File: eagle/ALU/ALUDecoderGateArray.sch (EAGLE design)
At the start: 0 parts

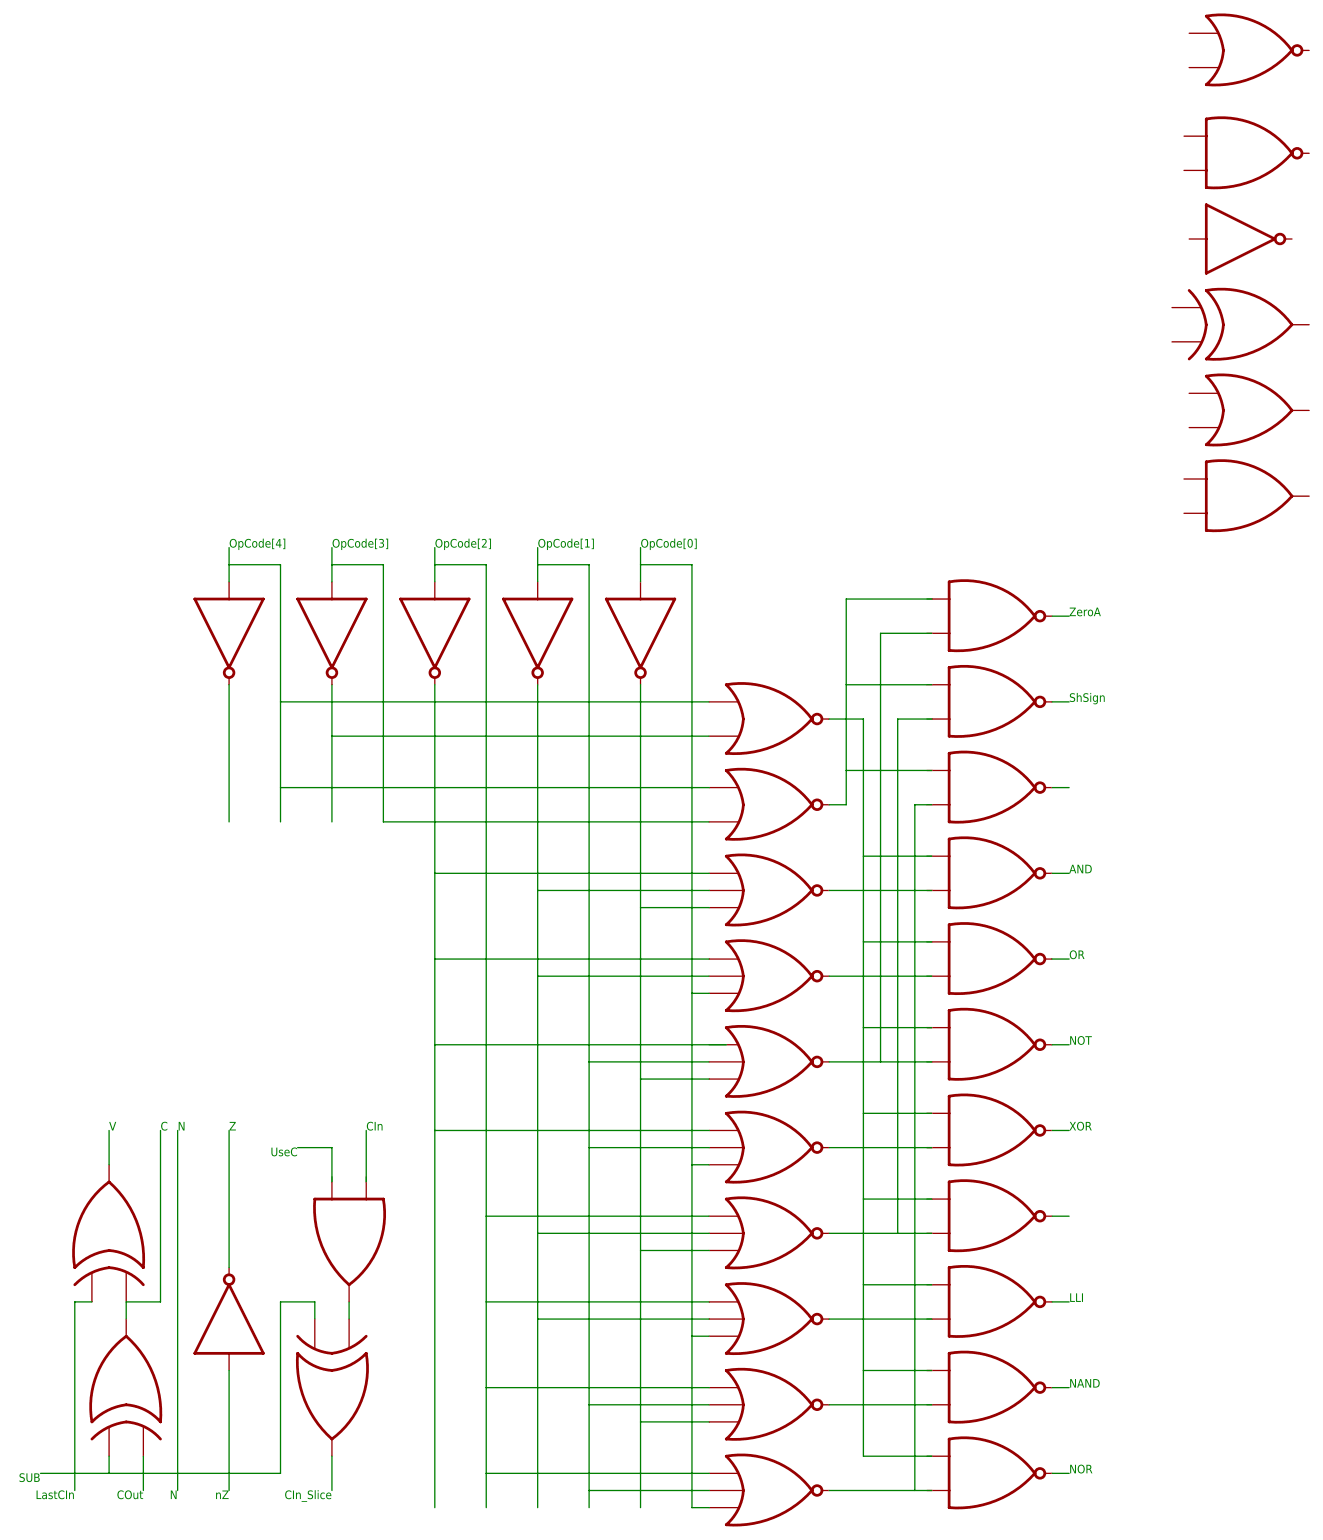
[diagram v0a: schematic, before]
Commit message: FR:ALU design reduction and rewording
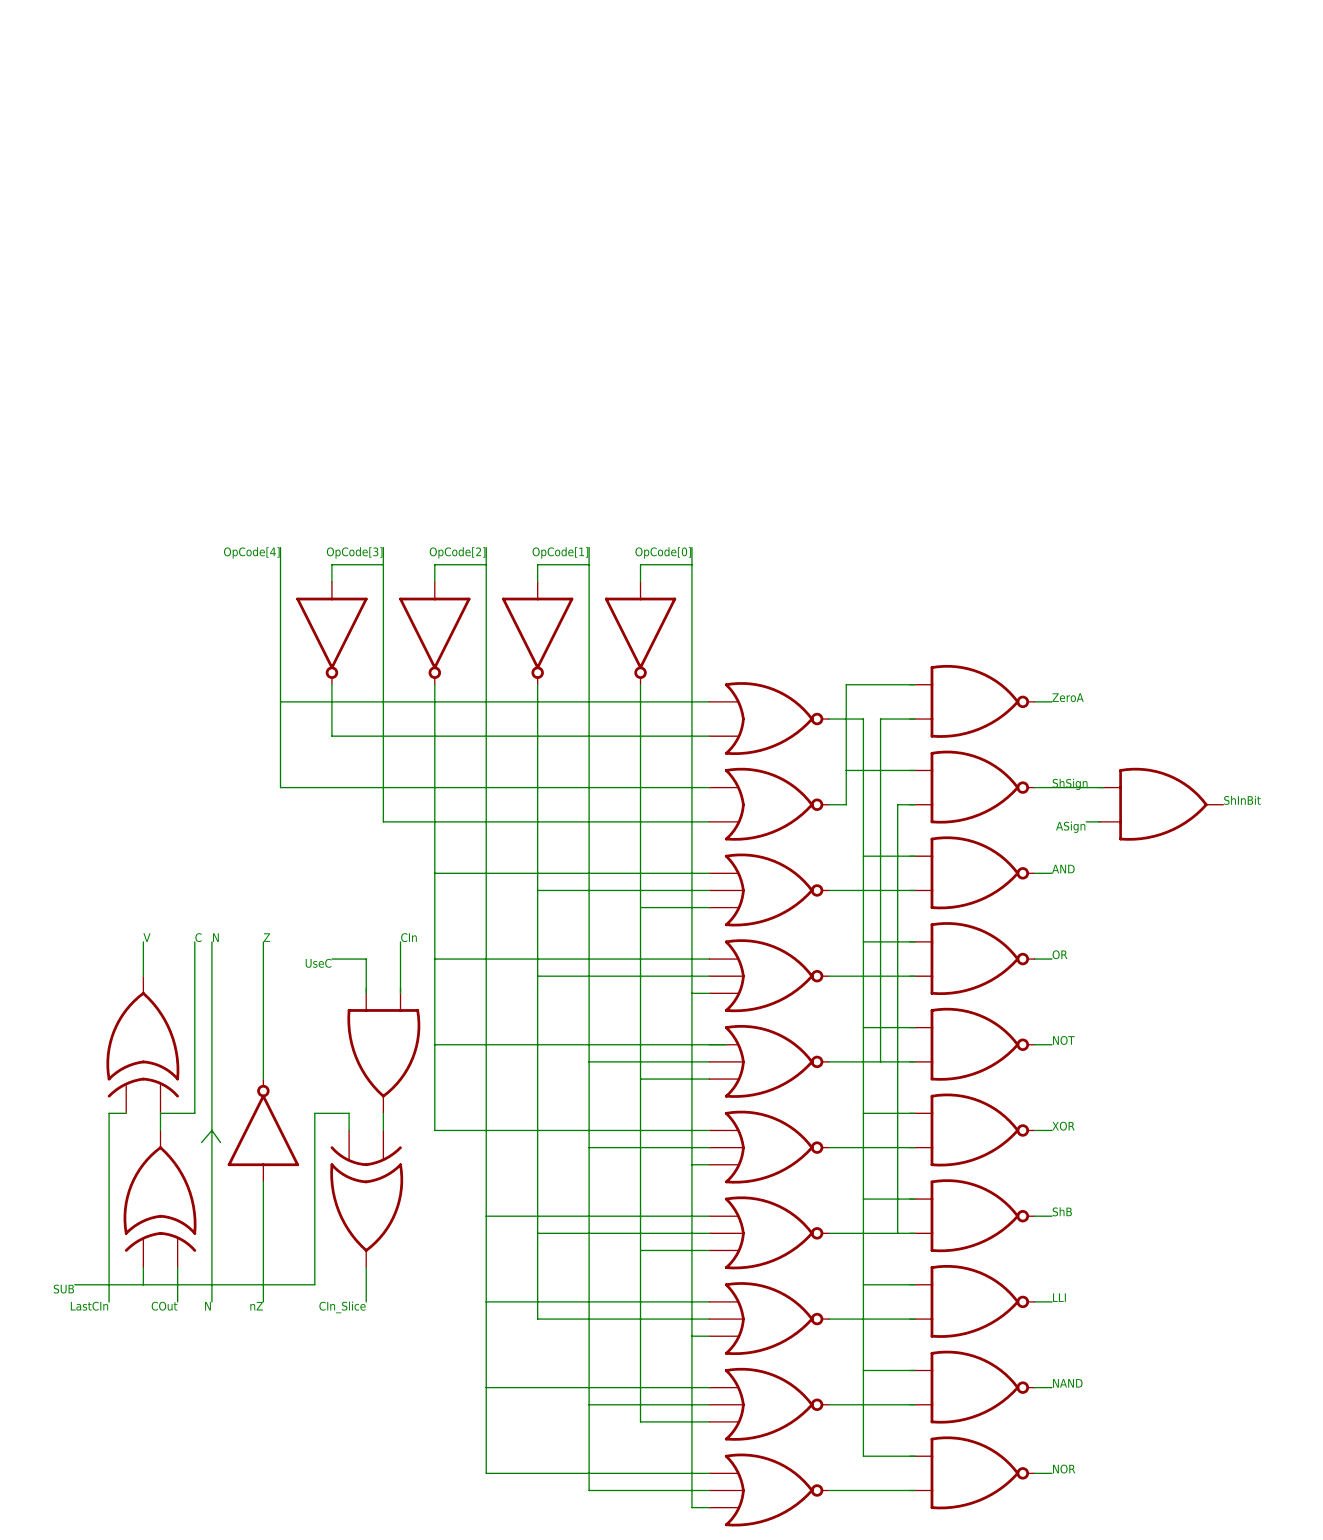
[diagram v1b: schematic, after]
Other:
- note added: "ASign"
- note added: "ShB"
- note added: "ShInBit"
